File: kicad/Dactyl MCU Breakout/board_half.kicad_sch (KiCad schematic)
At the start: 27 parts, among them J1 Columns, J2 Rows, J3 Thumbs, J4 Split, J5 Display, J6 External, J7 JST, J8 Split_extra, J9 Vic, SW1 Battery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

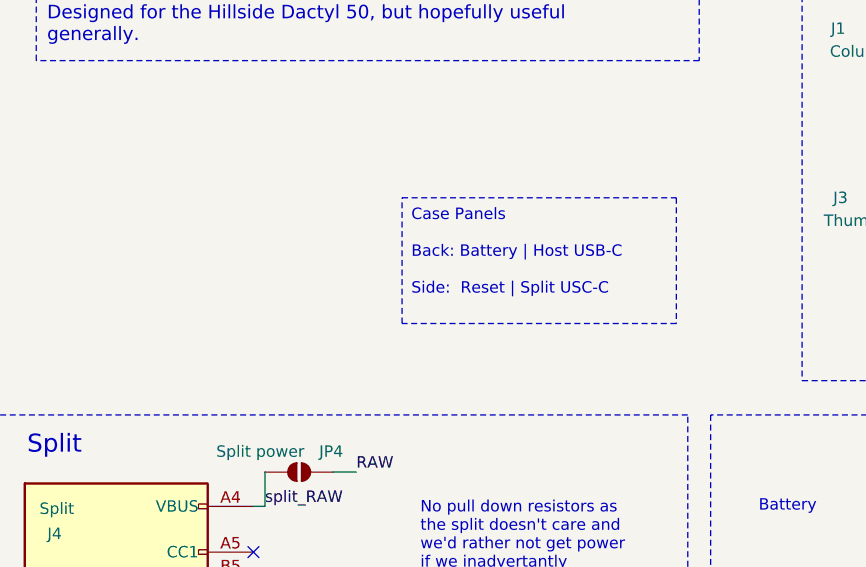
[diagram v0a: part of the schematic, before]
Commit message: feat: panel rails, back silk on footprints
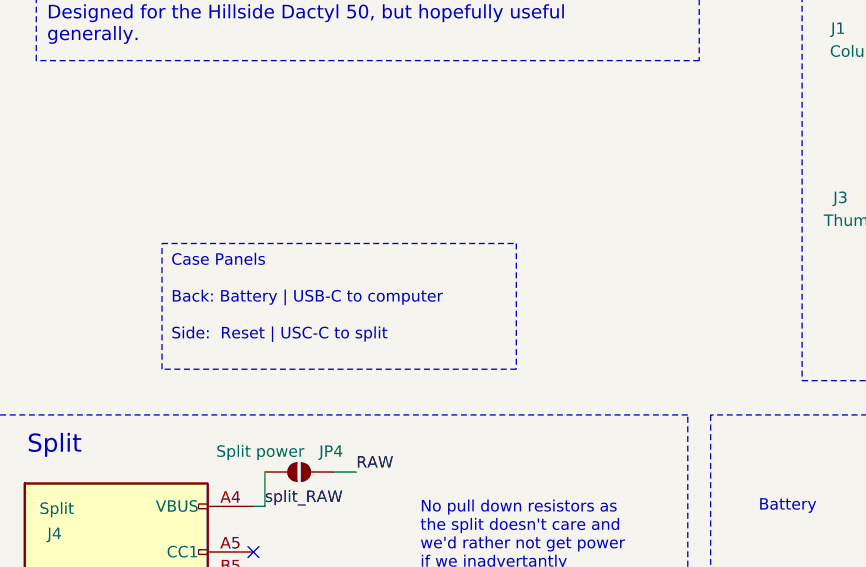
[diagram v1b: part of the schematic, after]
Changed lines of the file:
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@@
 		)
 	)
-	(text_box "        Case Panels\n\nBack: Battery | Host USB-C\n\nSide:  Reset | Split USC-C "
+	(text_box "        Case Panels\n\nBack: Battery | USB-C to computer\n\nSide:  Reset | USC-C to split"
 		(exclude_from_sim no)
-		(at 58.42 82.55 0)
-		(size 30.48 13.97)
+		(at 31.75 87.63 0)
+		(size 39.37 13.97)
 		(stroke
 			(width 0)

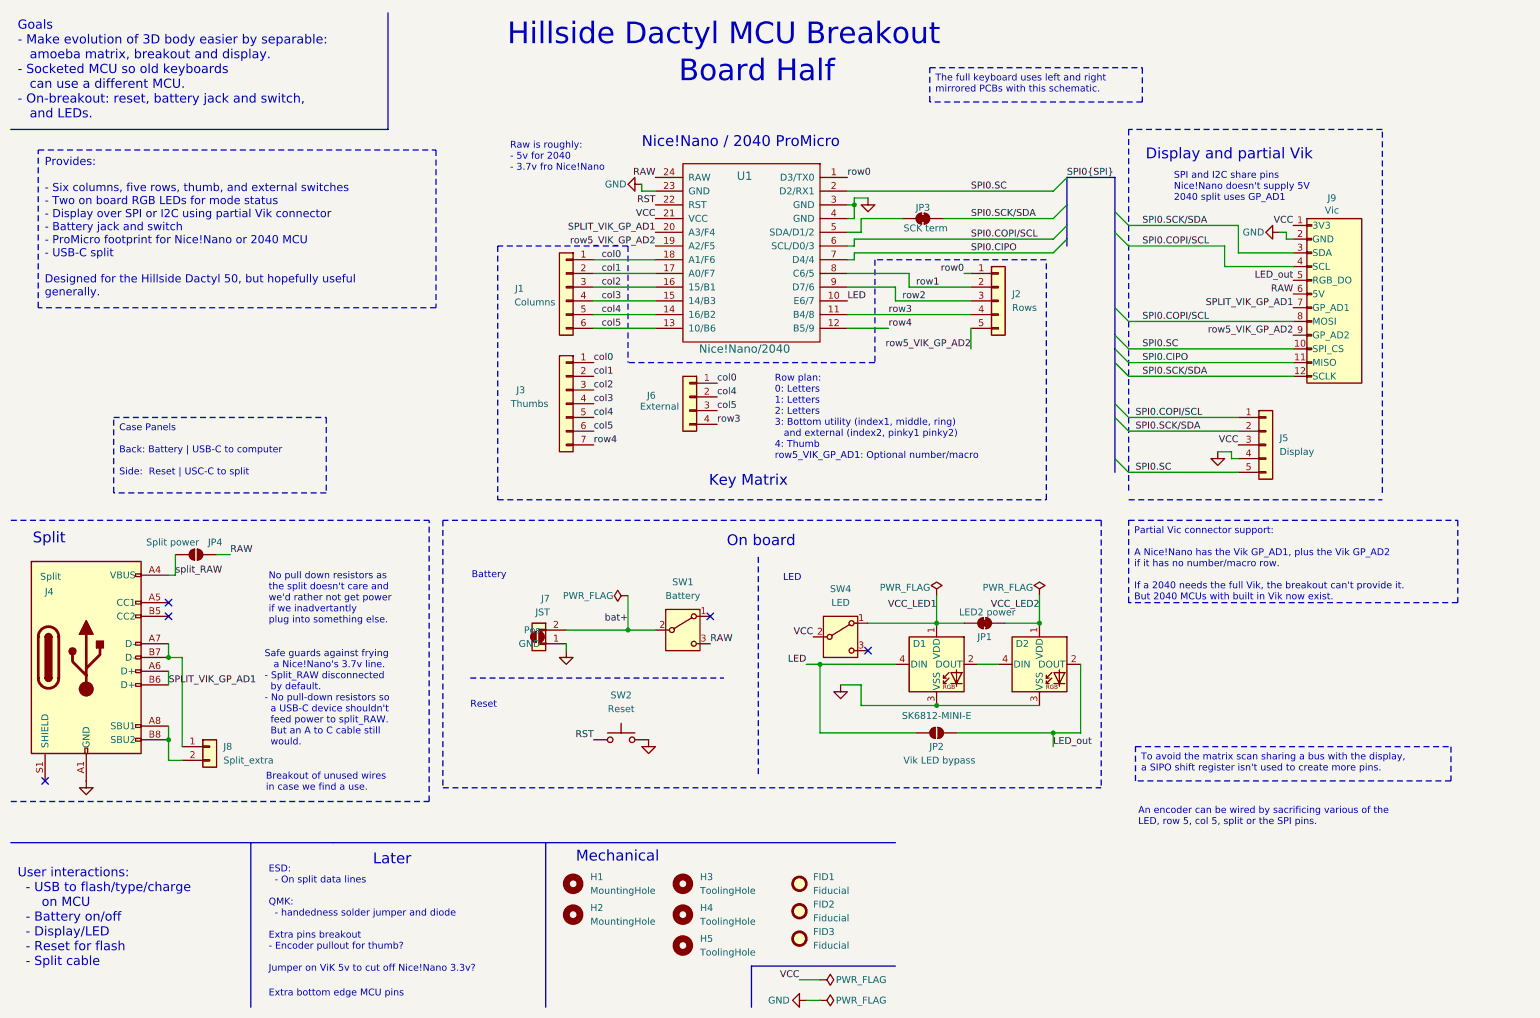
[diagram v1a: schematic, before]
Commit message: feat: Handedness jumper, better case corner notch
- Move panel details to separate project
- Remove Col 0 from thumb header
- Add handedness solder jumper and diode
- Add corner notch for case bottom mount
- Clean up silks and wiring
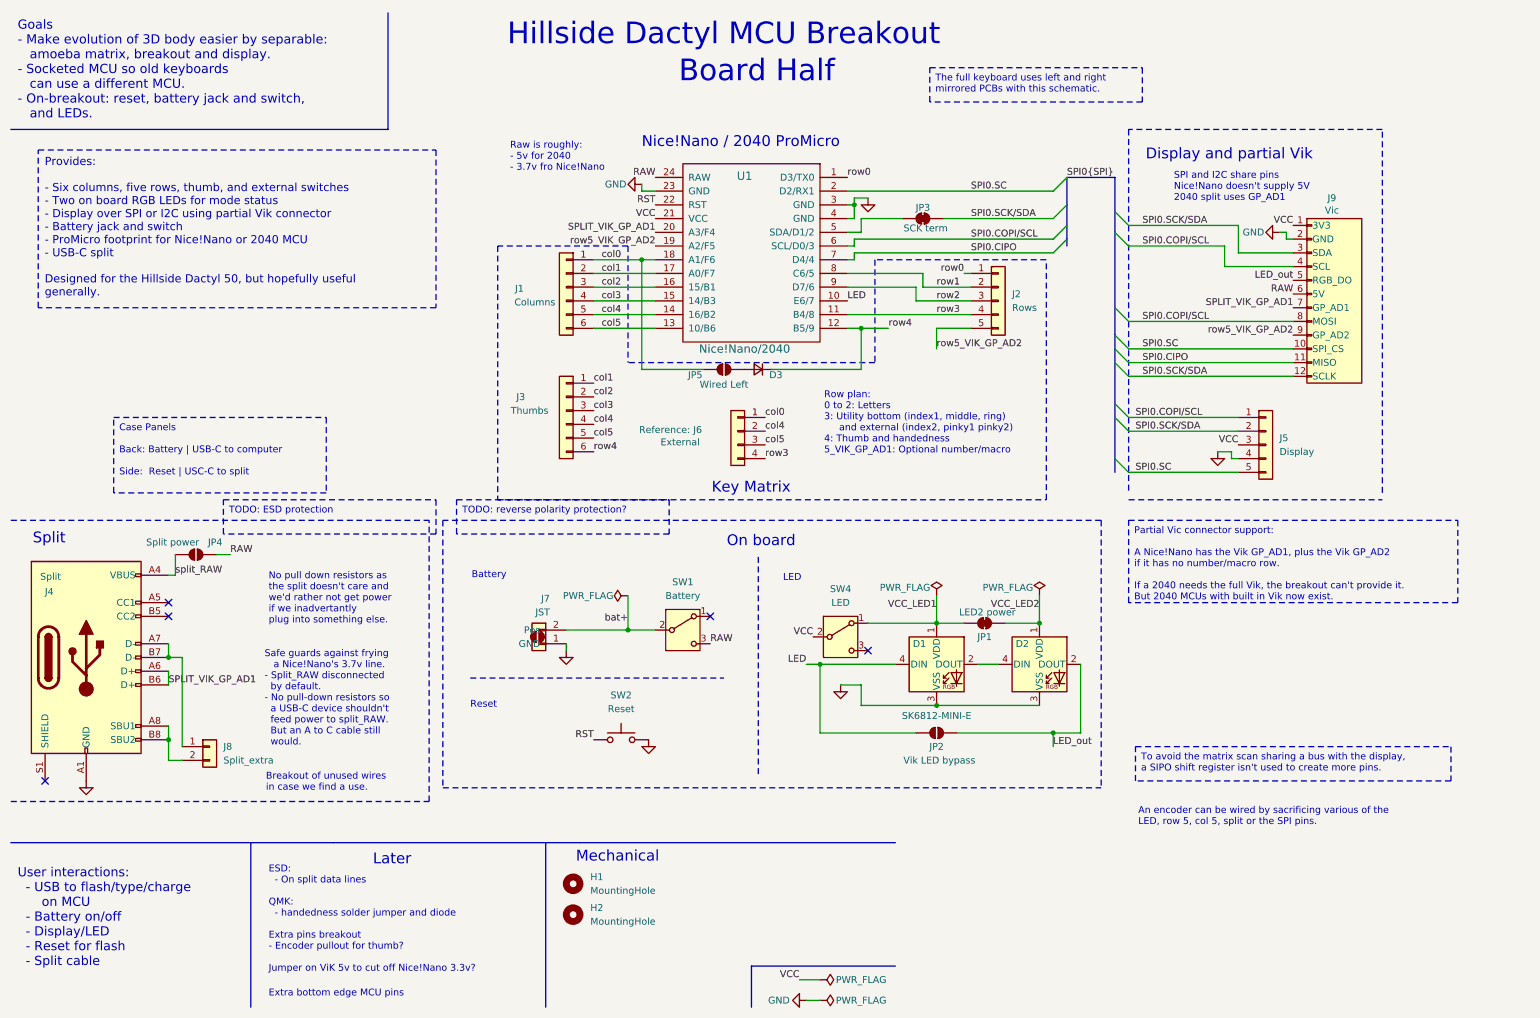
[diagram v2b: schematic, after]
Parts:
- removed FID1, FID2, FID3: Fiducial, Fiducial:Fiducial_1mm_Mask2mm, symbol Mechanical:Fiducial
- removed H3, H4, H5: ToolingHole, Dactyl:ToolingHole_1.152mm, symbol Mechanical:MountingHole
- added D3: D_Small, Diode_SMD:D_0603_1608Metric, symbol Device:D_Small
- added JP5: Wired Left, Jumper:SolderJumper-2_P1.3mm_Open_RoundedPad1.0x1.5mm, symbol Jumper:SolderJumper_2_Open
- J3: footprint Connector_PinHeader_2.54mm:PinHeader_1x07_P2.54mm_Vertical -> Dactyl:PinHeader_Thumbs; symbol Connector_Generic:Conn_01x07 -> Connector_Generic:Conn_01x06
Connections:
- net col0: now also JP5.1 (A); no longer J3.1 (Pin_1)
- net col1: now also J3.1 (Pin_1); no longer J3.2 (Pin_2)
- net col2: now also J3.2 (Pin_2); no longer J3.3 (Pin_3)
- net col3: now also J3.3 (Pin_3); no longer J3.4 (Pin_4)
- net col4: now also J3.4 (Pin_4); no longer J3.5 (Pin_5)
- net col5: now also J3.5 (Pin_5); no longer J3.6 (Pin_6)
- net row4: now also J3.6 (Pin_6), D3.1 (K); no longer J3.7 (Pin_7)
- new net: D3.2 (A), JP5.2 (B)
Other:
- note added: "Row plan: 0 to 2: Letters 3: Utility bottom (index1, middle, ring) and external (index2, pinky1 pinky2) 4: Thumb and handedness 5_VIK_GP_AD1: Optional number/macro"
- note removed: "Row plan: 0: Letters 1: Letters 2: Letters 3: Bottom utility (index1, middle, ring) and external (index2, pinky1 pinky2) 4: Thumb row5_VIK_GP_AD1: Optional number/macro"
- moved on the sheet: Reference: J6

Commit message: feat: ESD protection. Tidy up before mirroring
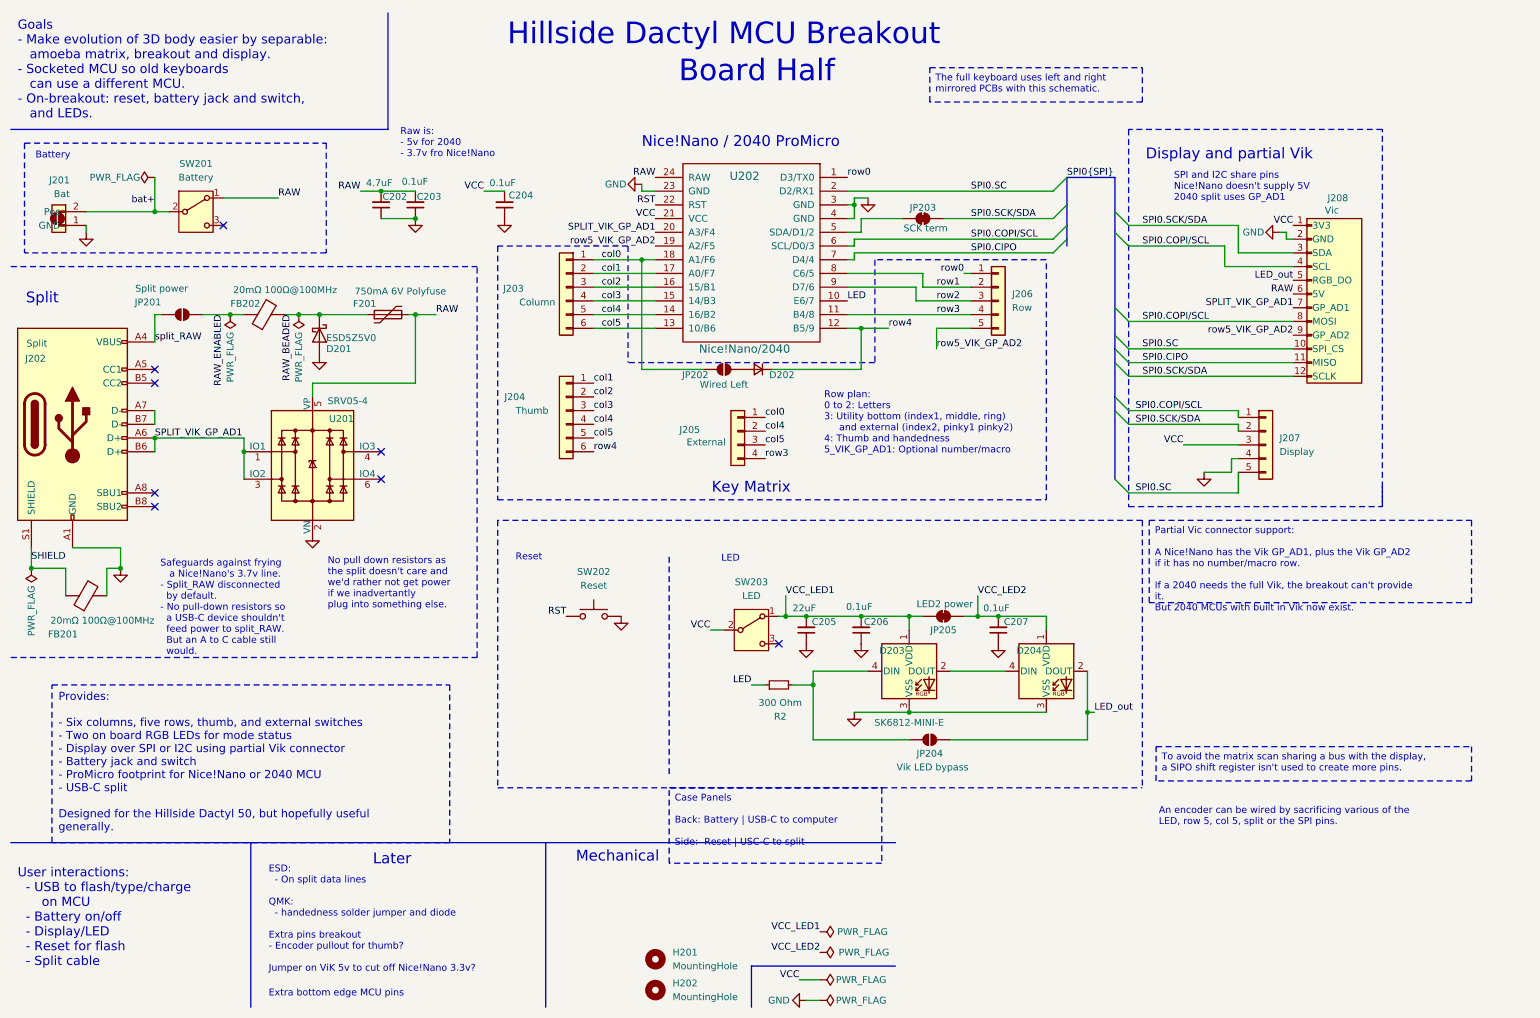
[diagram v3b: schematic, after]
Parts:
- removed J8: Split_extra, Connector_PinHeader_2.54mm:PinHeader_1x02_P2.54mm_Vertical, symbol Connector_Generic:Conn_01x02
- added C202: 4.7uF, Capacitor_SMD:C_0805_2012Metric, symbol Device:C_Small
- added C203, C204, C206, C207: 0.1uF, Capacitor_SMD:C_0402_1005Metric, symbol Device:C_Small
- added C205: 22uF, Capacitor_SMD:C_0805_2012Metric, symbol Device:C_Small
- added D201: ESD5Z5V0, Diode_SMD:D_SOD-523, symbol Diode:C3D12065A
- added F201: 750mA 6V Polyfuse, Fuse:Fuse_0805_2012Metric, symbol Device:Polyfuse
- added FB201, FB202: 20mΩ 100Ω@100MHz, Inductor_SMD:L_0805_2012Metric, symbol Device:FerriteBead
- added R2: 300 Ohm, Resistor_SMD:R_0603_1608Metric, symbol Device:R_Small
- added U201: SRV05-4, Package_TO_SOT_SMD:SOT-23-6, symbol Power_Protection:SRV05-4
- D202: renamed from D3; footprint Diode_SMD:D_0603_1608Metric -> Dactyl_basics:D_0603_1608Metric
- H201: renamed from H1; footprint MountingHole:MountingHole_3.2mm_M3_DIN965 -> Dactyl_basics:MountingHole_3.2mm_M3_DIN965; now left out of the parts list
- H202: renamed from H2; footprint MountingHole:MountingHole_3.2mm_M3_DIN965 -> Dactyl_basics:MountingHole_3.2mm_M3_DIN965; now left out of the parts list
- J201: renamed from J7; value JST -> Bat
- J202: renamed from J4; footprint Connector_USB:USB_C_Receptacle_HRO_TYPE-C-31-M-12 -> Dactyl_basics:USB_C_Receptacle_HRO_TYPE-C-31-M-12
- J203: renamed from J1; value Columns -> Column; footprint Connector_PinHeader_2.54mm:PinHeader_1x06_P2.54mm_Vertical -> Dactyl:PinHeader_Columns; now left out of the parts list
- J204: renamed from J3; value Thumbs -> Thumb; now left out of the parts list
- J205: renamed from J6; footprint Connector_PinHeader_2.54mm:PinHeader_1x04_P2.54mm_Vertical -> Dactyl:PinHeader_External; now left out of the parts list
- J206: renamed from J2; value Rows -> Row; footprint Connector_PinHeader_2.54mm:PinHeader_1x05_P2.54mm_Vertical -> Dactyl:PinHeader_Rows; now left out of the parts list
- J207: renamed from J5; footprint Connector_PinHeader_2.54mm:PinHeader_1x05_P2.54mm_Vertical -> Dactyl:PinHeader_Display; now left out of the parts list
- JP201: renamed from JP4; footprint Jumper:SolderJumper-2_P1.3mm_Open_RoundedPad1.0x1.5mm -> Dactyl_basics:SolderJumper-2_P1.3mm_Open_RoundedPad1.0x1.5mm
- JP202: renamed from JP5; footprint Jumper:SolderJumper-2_P1.3mm_Open_RoundedPad1.0x1.5mm -> Dactyl_basics:SolderJumper-2_P1.3mm_Open_RoundedPad1.0x1.5mm
- JP203: renamed from JP3; footprint Jumper:SolderJumper-2_P1.3mm_Bridged_RoundedPad1.0x1.5mm -> Dactyl_basics:SolderJumper-2_P1.3mm_Bridged_RoundedPad1.0x1.5mm
- JP204: renamed from JP2; footprint Jumper:SolderJumper-2_P1.3mm_Open_RoundedPad1.0x1.5mm -> Dactyl_basics:SolderJumper-2_P1.3mm_Open_RoundedPad1.0x1.5mm
- JP205: renamed from JP1; footprint Jumper:SolderJumper-2_P1.3mm_Bridged_RoundedPad1.0x1.5mm -> Dactyl_basics:SolderJumper-2_P1.3mm_Bridged_RoundedPad1.0x1.5mm; now left out of the parts list
- SW201: renamed from SW1; footprint Dactyl:SW_SPDT_JS202011AQN_wider -> Dactyl:SW_SPDT_Battery
- SW202: renamed from SW2; footprint Dactyl:SW_Tactile_SKHL_Angled -> Dactyl_basics:SW_Tactile_SKHL_Angled
- renumbered D1 to D203, D2 to D204, J9 to J208, SW4 to SW203, U1 to U202
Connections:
- net GND: now also C202.1, C203.1, C204.1, C205.1, C206.1, C207.1, D201.2 (A), FB201.2, U201.2 (VN)
- net LED: now also R2.1; no longer D203.4 (DIN), JP204.1 (A)
- net RAW: now also SW201.1 (A), C202.2, C203.2, F201.2, U201.5 (VP); no longer JP201.2 (B), SW201.3 (C)
- net SPLIT_VIK_GP_AD1: now also U201.1 (IO1), U201.3 (IO2)
- net VCC: now also C204.2
- net VCC_LED1: now also C205.2, C206.2
- net VCC_LED2: now also C207.2
- net at J202.A8 (SBU1): no longer J202.B8 (SBU2)
- net SHIELD: now reaches J202.S1 (SHIELD)
- net SHIELD: now also FB201.1
- new net: D203.4 (DIN), JP204.1 (A), R2.2
- new net RAW_BEADED: D201.1 (K), F201.1, FB202.2
- new net RAW_ENABLED: FB202.1, JP201.2 (B)
- no-connect marks 5 -> 8
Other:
- note added: "Raw is: - 5v for 2040 - 3.7v fro Nice!Nano"
- note added: "Safeguards against frying a Nice!Nano's 3.7v line. - Split_RAW disconnected by default. - No pull-down resistors so a USB-C device shouldn't feed power to split_RAW. But an A to C cable still would."
- note removed: "Breakout of unused wires in case we find a use."
- note removed: "On board"
- note removed: "Raw is roughly: - 5v for 2040 - 3.7v fro Nice!Nano"
- note removed: "Safe guards against frying a Nice!Nano's 3.7v line. - Split_RAW disconnected by default. - No pull-down resistors so a USB-C device shouldn't feed power to split_RAW. But an A to C cable still would."
- moved on the sheet: D203, D204, H201, H202, J201, J202, JP201, JP204, JP205, SW201, SW202, SW203
